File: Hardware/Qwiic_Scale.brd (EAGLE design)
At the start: 25.4 x 35.6 mm, 68 parts, among them J2 Qwiic Right Angle, J3 PTH, J4 Qwiic Right Angle, J7 Spring Terminal, U1 NAU7802

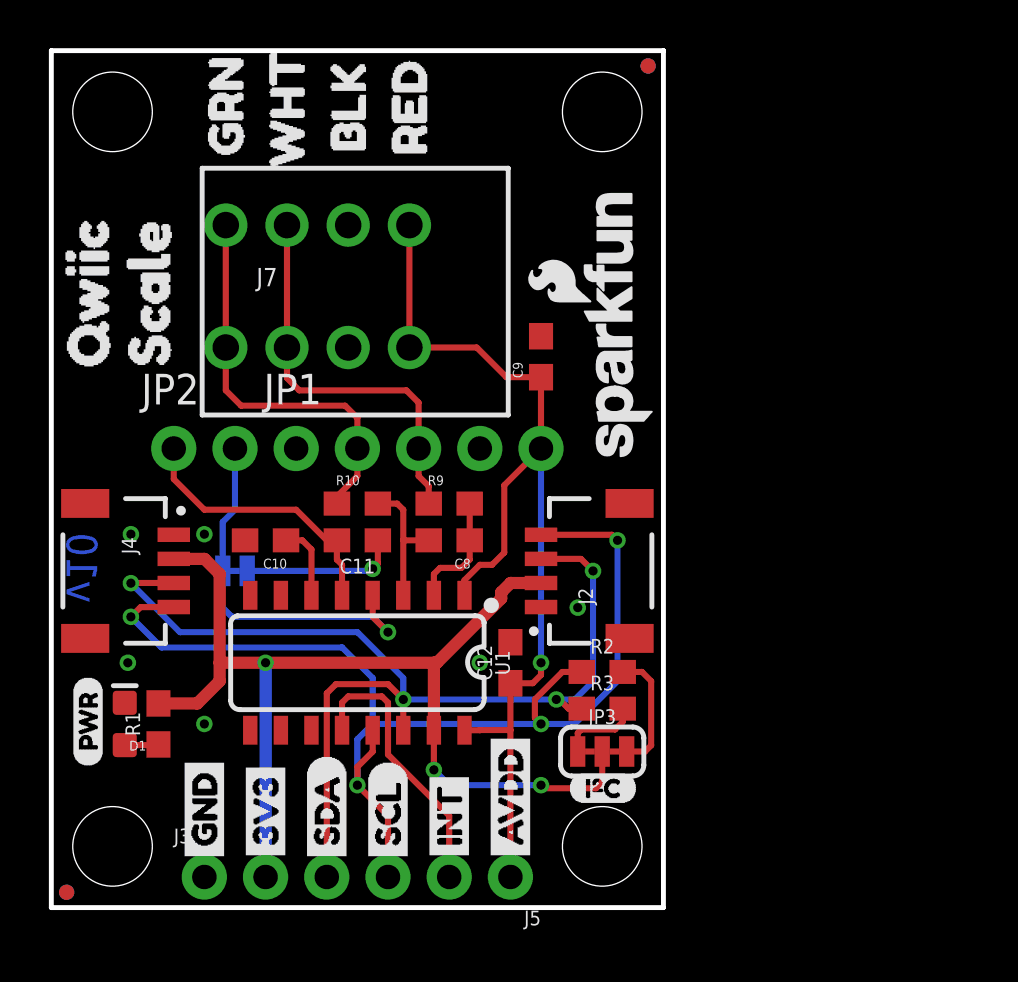
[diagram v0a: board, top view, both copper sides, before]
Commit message: Silk change to terminal. Better ground ties.
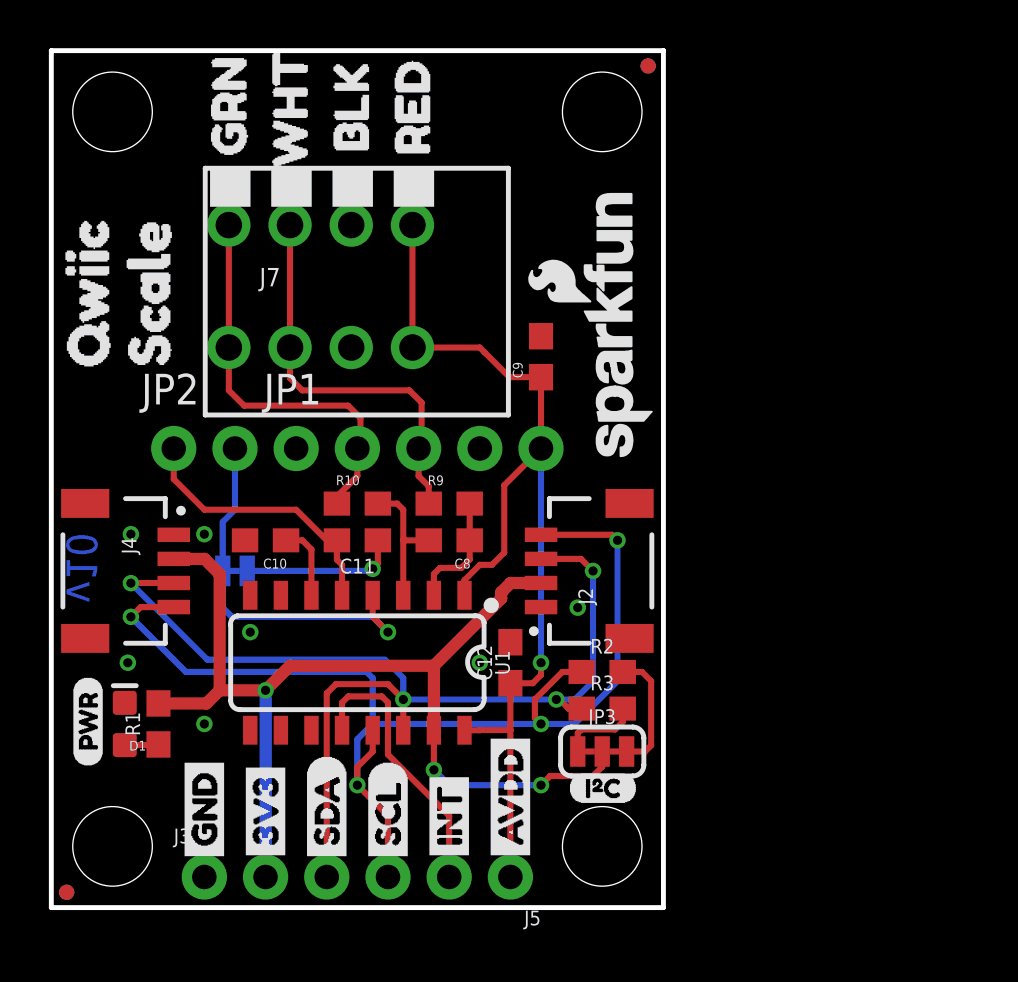
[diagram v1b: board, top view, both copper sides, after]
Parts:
- removed U$14: (no value), buzzard_labels (69):J10
- added U$20: (no value), buzzard_labels (15):CAP0
- J1: value (none) -> CAP
- moved U$39 3.30 mm to (7.37, 28.4)
- moved U$43 3.18 mm to (9.91, 28.2)
- moved U$30 1.94 mm to (20.3, 25.4), turned to 90 degrees
- moved U$41 0.13 mm to (15.0, 30.0)
- moved U$42 0.13 mm to (15.0, 30.4)
- moved U$44 0.13 mm to (9.91, 29.5)
- moved J7 0.13 mm to (7.37, 25.8)
- moved U$40 0.13 mm to (7.37, 30.0)
- moved U$37 0.13 mm to (12.4, 29.0)
- moved U$38 0.13 mm to (12.4, 30.1)
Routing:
- net 3.3V: track 46.4 -> 45.3 mm
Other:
- board text added: "N. Seidle"
- board text added: "Units in inches"

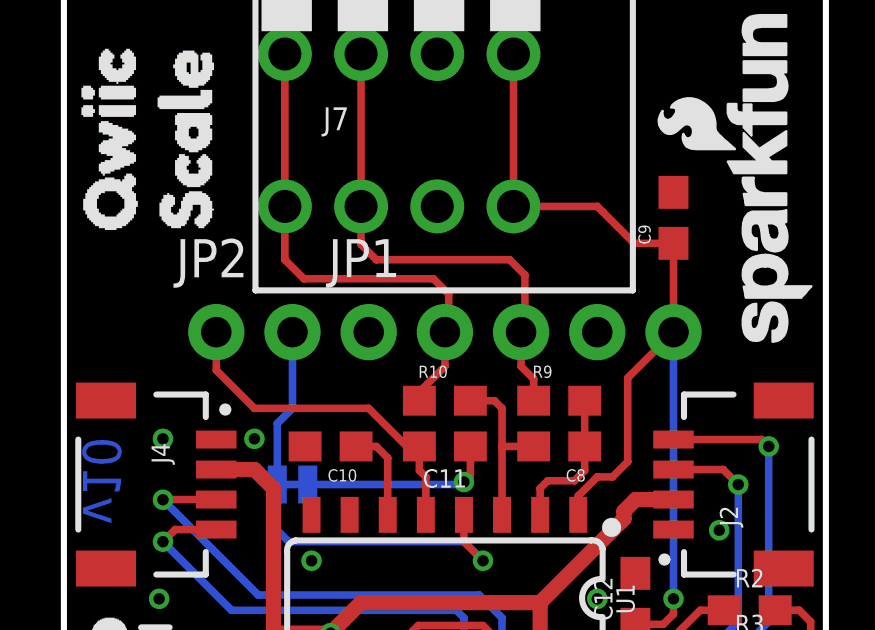
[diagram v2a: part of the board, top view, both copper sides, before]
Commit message: Divided schematic. Added VDD range.
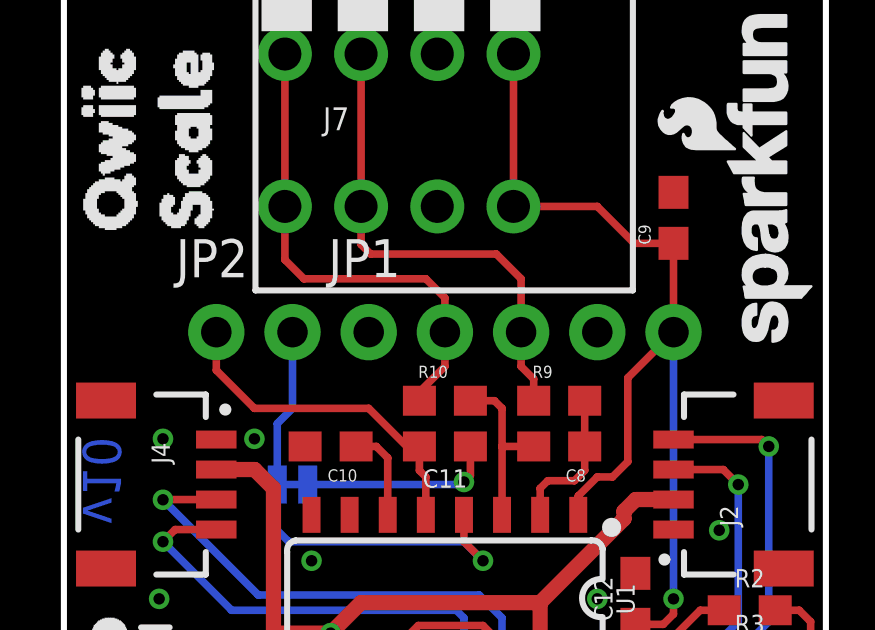
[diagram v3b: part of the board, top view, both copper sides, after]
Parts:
- J2, J4: value Qwiic Right Angle -> Qwiic

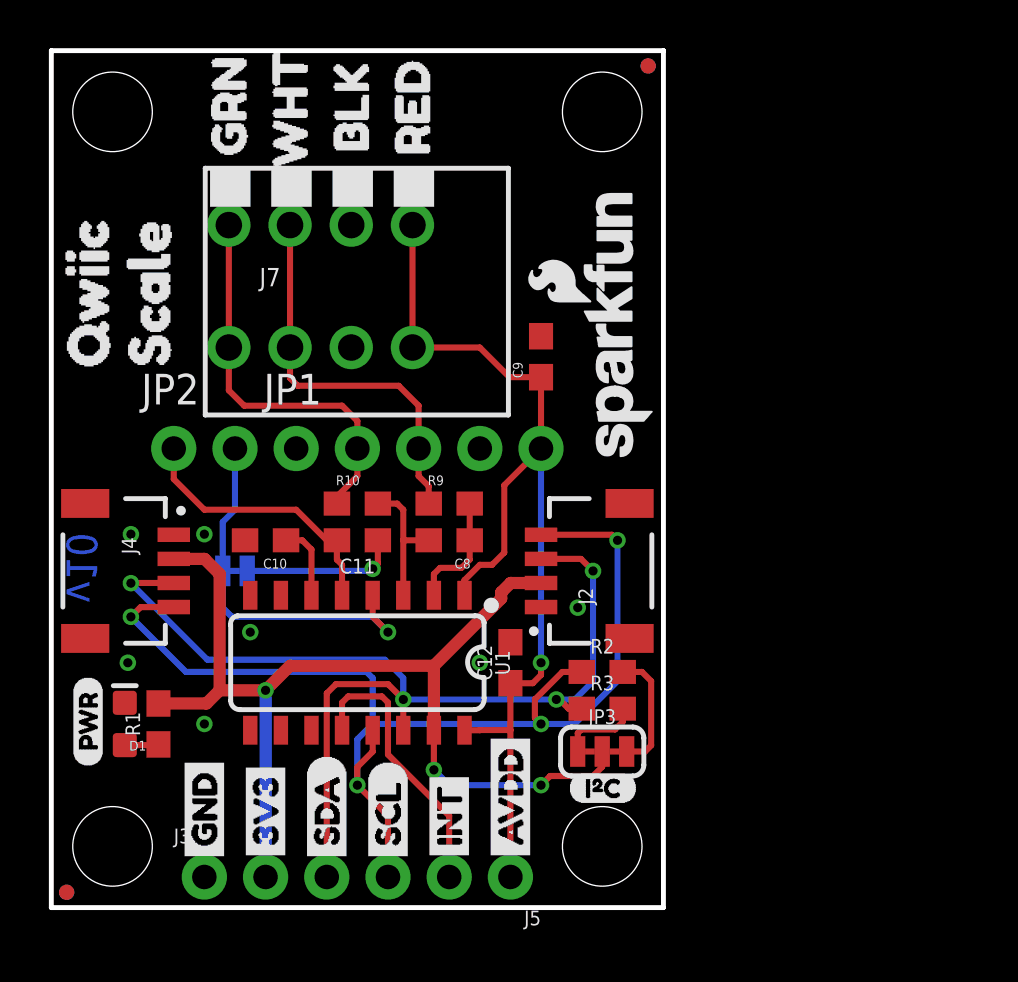
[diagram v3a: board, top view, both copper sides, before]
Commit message: Divided schematic. Added VDD range.
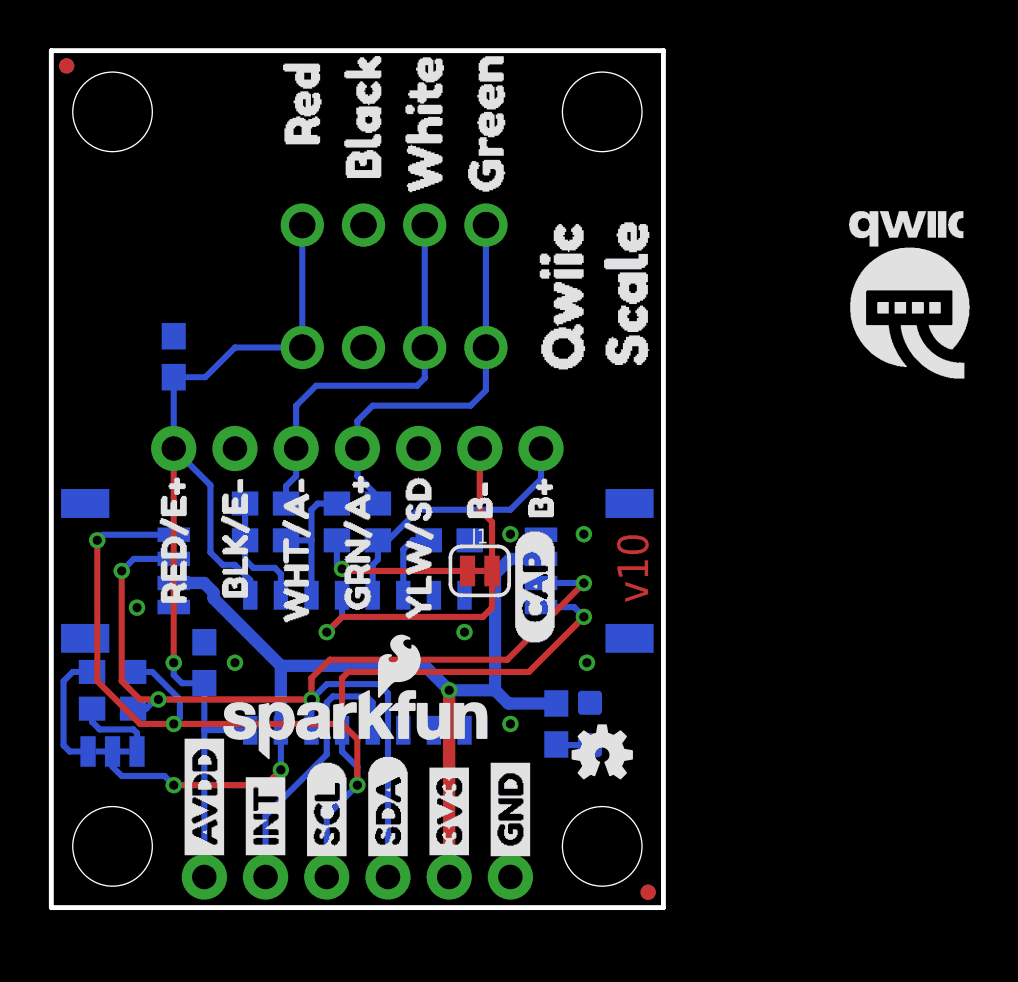
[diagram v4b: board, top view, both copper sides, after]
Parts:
- moved FRAME1 61.0 mm to (43.2, -17.8), flipped to the bottom
- moved JP21 24.1 mm to (0.64, 34.9), flipped to the bottom
- moved JP61 24.1 mm to (24.8, 0.64), flipped to the bottom
- moved JP71 24.1 mm to (0.64, 34.9), flipped to the top
- moved JP81 24.1 mm to (24.8, 0.64), flipped to the top
- moved U$18 22.4 mm to (23.9, 5.84), flipped to the bottom
- moved U$22 22.4 mm to (23.9, 21.0), flipped to the bottom
- moved U$25 22.4 mm to (23.9, 21.0), flipped to the top
- moved LOGO3 21.6 mm to (1.91, 24.3), flipped to the bottom
- moved JP101 20.3 mm to (2.54, 33.0), flipped to the bottom
- moved JP3 20.3 mm to (2.54, 6.48), flipped to the bottom
- moved JP31 20.3 mm to (22.9, 2.54), flipped to the bottom
- moved JP41 20.3 mm to (22.9, 33.0), flipped to the bottom
- moved JP91 20.3 mm to (2.54, 2.54), flipped to the bottom
- moved LOGO1 20.3 mm to (22.9, 6.35), flipped to the top
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
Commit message: Update Qwiic logo. Remove old panel files.
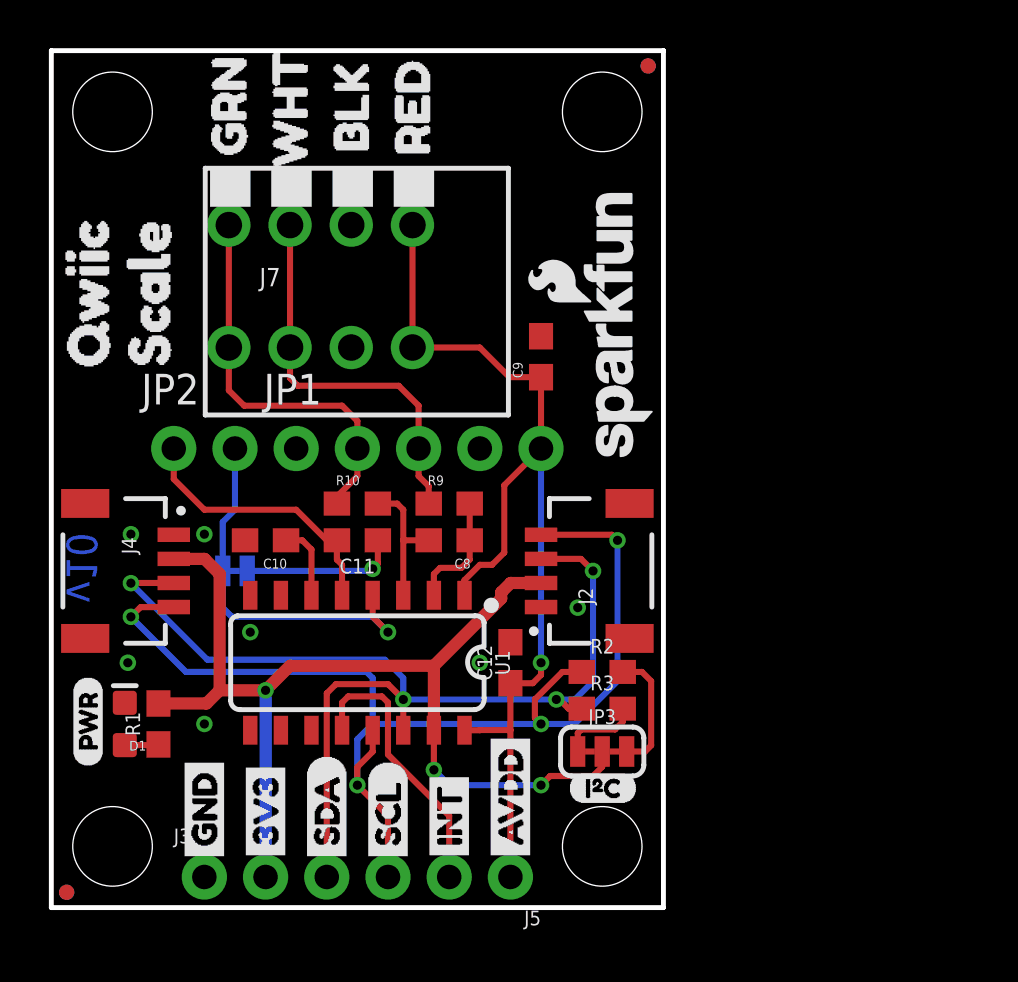
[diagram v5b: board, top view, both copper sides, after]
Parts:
- removed U$25: (no value), buzzard_labels (68):SCALE3
- removed U$30: (no value), Labels:QWIIC-LOGO-MEDIUM
- added U$14: (no value), buzzard_labels (68):QWIIC2
- added U$26: QWIIC_LOGO_8MM, Qwiic_Logo:QWIIC_8MM
- U$17: device buzzard_labels (68):QWIIC2 -> buzzard_labels (68):SCALE3
- moved FRAME1 61.0 mm to (-17.8, -17.8), flipped to the top
- moved JP21 24.1 mm to (24.8, 34.9), flipped to the top
- moved JP61 24.1 mm to (0.64, 0.64), flipped to the top
- moved JP71 24.1 mm to (24.8, 34.9), flipped to the bottom
- moved JP81 24.1 mm to (0.64, 0.64), flipped to the bottom
- moved U$18 22.4 mm to (1.52, 5.84), flipped to the top
- moved U$22 22.4 mm to (1.52, 21.0), flipped to the top
- moved LOGO3 21.6 mm to (23.5, 24.3), flipped to the top
- moved JP101 20.3 mm to (22.9, 33.0), flipped to the top
- moved JP3 20.3 mm to (22.9, 6.48), flipped to the top
- moved JP31 20.3 mm to (2.54, 2.54), flipped to the top
- moved JP41 20.3 mm to (2.54, 33.0), flipped to the top
- moved JP91 20.3 mm to (22.9, 2.54), flipped to the top
- moved LOGO1 20.3 mm to (2.54, 6.35), flipped to the bottom
- moved R2 20.3 mm to (22.9, 9.78), flipped to the top
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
